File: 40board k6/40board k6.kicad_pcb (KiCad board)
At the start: 2 copper layers, 10.1 x 6.4 mm, 111 parts, among them J1 USB_C_Receptacle_USB2.0, SW1 SW_Push, SW2 RotaryEncoder, U1 ATmega32U4-M, Y1 16MHz

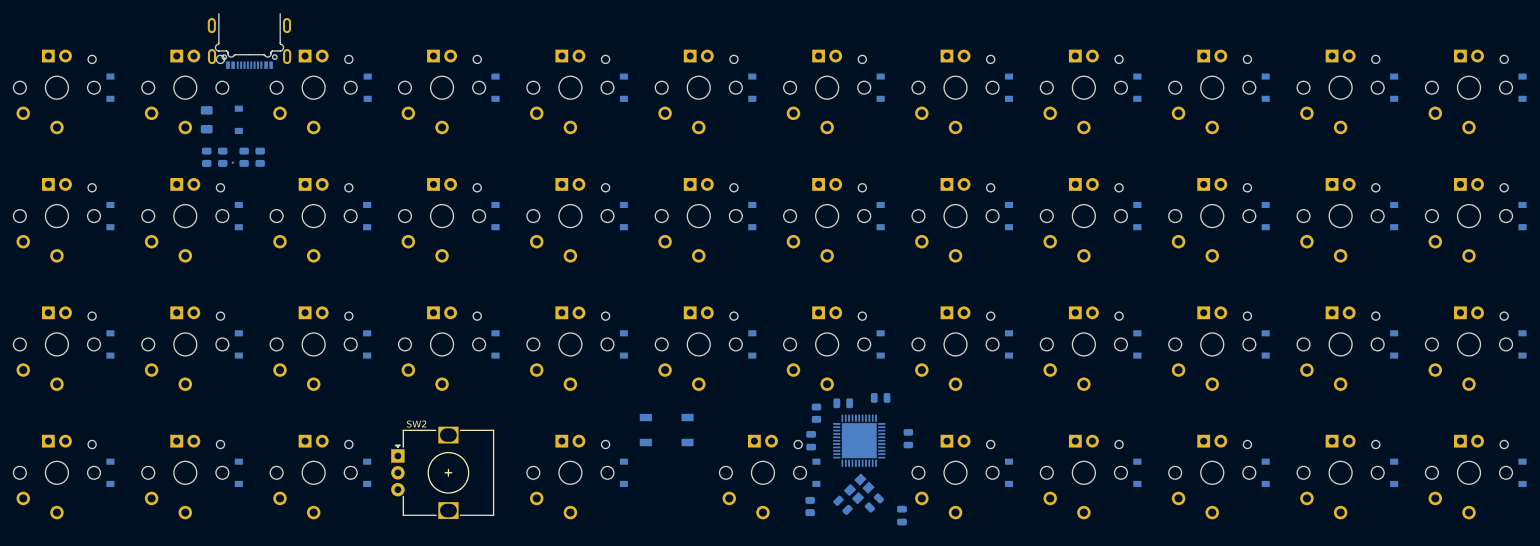
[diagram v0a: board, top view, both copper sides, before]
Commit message: Finished routing PCB
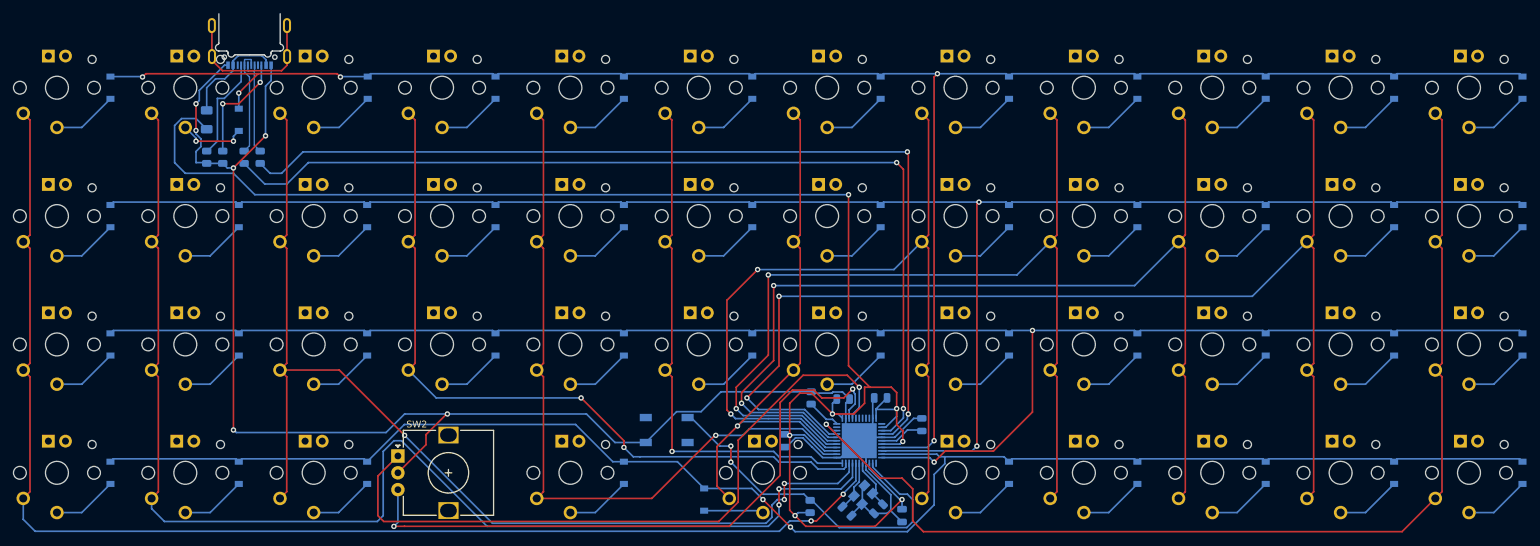
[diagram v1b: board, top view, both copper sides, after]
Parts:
- moved D26 17.1 mm to (351.6, 126.2)
- moved C3 3.97 mm to (363.5, 117.5)
- moved C7 2.89 mm to (383.9, 115.1)
- moved R4 2.40 mm to (367.5, 111.1)
- moved Y1 1.06 mm to (375.2, 125.5)
- moved C4 1.06 mm to (372.8, 127.9)
- moved C5 1.06 mm to (377.5, 127.6)
- moved C1 0.62 mm to (372.3, 111.3)
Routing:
- net Row 0: track 0.00 -> 282.4 mm, vias 0 -> 5
- net Row 1: track 0.00 -> 264.2 mm, vias 0 -> 2
- net GND: track 0.00 -> 253.8 mm, vias 0 -> 6
- net Row 2: track 0.00 -> 251.3 mm, vias 0 -> 2
- net +5V: track 0.00 -> 246.0 mm, vias 0 -> 7
- net Row 3: track 0.00 -> 238.2 mm, vias 0 -> 2
- net Col 0: track 0.00 -> 192.9 mm, vias 0 -> 2
- net Col 1: track 0.00 -> 189.2 mm, vias 0 -> 2
- net Col 10: track 0.00 -> 173.9 mm, vias 0 -> 2
- net Col 11: track 0.00 -> 163.4 mm, vias 0 -> 1
- net Col 2: track 0.00 -> 160.5 mm, vias 0 -> 3
- net Col 9: track 0.00 -> 158.1 mm, vias 0 -> 2
- net Net-(R2-Pad2): track 0.00 -> 142.5 mm, vias 0 -> 2
- net Col 8: track 0.00 -> 142.2 mm, vias 0 -> 2
- net Net-(R1-Pad2): track 0.00 -> 141.7 mm, vias 0 -> 2
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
